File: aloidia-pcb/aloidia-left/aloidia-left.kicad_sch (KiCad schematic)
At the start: 81 parts

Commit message: Finished schematics of left half
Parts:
- removed J?: SWD 10 Pin 0.05", 0_various:FTSH-105-01, symbol 0_various:SWD 10 Pin 0.05"
- added C10, C11, C12, C13: 0.1uF, symbol Device:C_Small
- added D100, D101, D102, D103, D104, D105, D106, D107, D108, D110, D111, D112, D113, D114, D115, D116, D117, D120, D121, D122, D123, D124, D125, D126, D127, D130, D131, D132, D133, D134, D135, D136, D137, D140, D141, D142, D143, D144, D145, D146, D147, D2, D3, D4, D5, D6: 1N4148W, Diode_SMD:D_SOD-123, symbol Diode:1N4148W
- added FB2: MH2029-600Y, Inductor_SMD:L_0805_2012Metric, symbol 0_protection:MH2029-600Y
- added H1: 3.2mm_M3, MountingHole:MountingHole_3.2mm_M3_Pad_Via, symbol Mechanical:MountingHole_Pad
- added H2, H3, H4: 3.2mm_M3, MountingHole:MountingHole_3.2mm_M3_Pad_Via, symbol Mechanical:MountingHole
- added J1: SWD_02x05_1.27mm, 0_various:FTSH-105-01, symbol 0_various:SWD_02x05_1.27mm
- added J2: Pin headers 2.54mm 01x08, Connector_PinHeader_2.54mm:PinHeader_1x08_P2.54mm_Vertical, symbol Connector_Generic:Conn_01x08
- added J3: SM06B-SRSS-TB, Connector_JST:JST_SH_SM06B-SRSS-TB_1x06-1MP_P1.00mm_Horizontal, symbol Connector_Generic:Conn_01x06
- added R6, R7: 10k, symbol Device:R_Small
- added SW100: MX_EC11, 0_mx:MX_HS_AS_EC11_1u, symbol Device:RotaryEncoder_Switch
- added SW101, SW102, SW103, SW104, SW105, SW106, SW107, SW108, SW110, SW111, SW112, SW113, SW114, SW115, SW116, SW117, SW120, SW121, SW122, SW123, SW124, SW125, SW126, SW127, SW130, SW131, SW132, SW133, SW134, SW135, SW136, SW137, SW140, SW141, SW142, SW143, SW144, SW145, SW146, SW243, SW244, SW246: SW_Push, symbol Switch:SW_Push
- added SW2: MX_EVQWGD001, 0_mx:MX_HS_AS_1u_EVQWGD001, symbol Device:RotaryEncoder_Switch
- added SW4: EG6201, 0_switch_button:SW_EG6201, symbol 0_switch_button:EG6201
- added TP1: 3.3V, 0_various:TestPoint, symbol Connector:TestPoint
- added TP10: SDA, 0_various:TestPoint, symbol Connector:TestPoint
- added TP11: EVQ_ENCB, 0_various:TestPoint, symbol Connector:TestPoint
- added TP12: EVQ_ENCA, 0_various:TestPoint, symbol Connector:TestPoint
- added TP13: EC_ENCB, 0_various:TestPoint, symbol Connector:TestPoint
- added TP14: EC_ENCA, 0_various:TestPoint, symbol Connector:TestPoint
- added TP15: RESET, 0_various:TestPoint, symbol Connector:TestPoint
- added TP16: ROW0, 0_various:TestPoint, symbol Connector:TestPoint
- added TP17: ROW1, 0_various:TestPoint, symbol Connector:TestPoint
- added TP18: ROW2, 0_various:TestPoint, symbol Connector:TestPoint
- added TP19: ROW3, 0_various:TestPoint, symbol Connector:TestPoint
- added TP2: VDD, 0_various:TestPoint, symbol Connector:TestPoint
- added TP20: ROW4, 0_various:TestPoint, symbol Connector:TestPoint
- added TP21: COL0, 0_various:TestPoint, symbol Connector:TestPoint
- added TP22: COL1, 0_various:TestPoint, symbol Connector:TestPoint
- added TP23: COL2, 0_various:TestPoint, symbol Connector:TestPoint
- added TP24: COL6, 0_various:TestPoint, symbol Connector:TestPoint
- added TP25: COL7, 0_various:TestPoint, symbol Connector:TestPoint
- added TP26: COL8, 0_various:TestPoint, symbol Connector:TestPoint
- added TP27: COL9, 0_various:TestPoint, symbol Connector:TestPoint
- added TP28, TP29, TP30, TP31, TP32: GND, lib_fp:TestPoint, symbol Connector:TestPoint
- added TP3: VDDH, 0_various:TestPoint, symbol Connector:TestPoint
- added TP33: COL3, 0_various:TestPoint, symbol Connector:TestPoint
- added TP34: COL4, 0_various:TestPoint, symbol Connector:TestPoint
- added TP35: COL5, 0_various:TestPoint, symbol Connector:TestPoint
- added TP4: VBUS, 0_various:TestPoint, symbol Connector:TestPoint
- added TP5: VBUS_ESD, 0_various:TestPoint, symbol Connector:TestPoint
- added TP6: VBUS_FUSE, 0_various:TestPoint, symbol Connector:TestPoint
- added TP7: SYSOFF, 0_various:TestPoint, symbol Connector:TestPoint
- added TP8: CHG, 0_various:TestPoint, symbol Connector:TestPoint
- added TP9: SCL, 0_various:TestPoint, symbol Connector:TestPoint
- D1: renamed from D?; value LED_BGRA -> IN-P32TRRRGB; footprint (none) -> 0_various:IN-P32TRRRGB; Manufacturer ref (none) -> IN-P32TRRRGB; Mouser ref (none) -> 743-IN-P32TRRRGB
- R10: renamed from R?; value 10k -> 1.27k
- R11: renamed from R?; value 10k -> 1.15k
- R12: renamed from R?; value 10k -> 1.4k
- gave numbers to parts that had none: 69
- renumbered RESET to RESET1
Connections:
- net +3.3V: now also J2.2 (Pin_2), TP1.1
- net CHG: now also TP8.1
- net D+: no longer U7.6 (IO4)
- net D-: no longer U7.4 (IO3)
- net GND: now also C10.2, C11.1, C12.2, C13.1, FB2.2, J1.3 (GND), J1.5 (GND), J2.1 (Pin_1), SW100.C, SW2.C, SW4.18, SW4.S1 (SHIELD), SW4.S2 (SHIELD), SW4.S3 (SHIELD), SW4.S4 (SHIELD), TP28.1, TP29.1, TP30.1, TP31.1, TP32.1
- net RESET: now also J1.10 (nRESET), TP15.1
- net SCL: now also U2.26 (TRACEDATA3/P1.09), R6.2, TP9.1
- net SDA: now also U2.27 (TRACEDATA2/P0.11), R7.2, TP10.1
- net SWCLK: now also J1.4 (SWCLK/TCK)
- net SWDIO: now also J1.2 (SWDIO/TMS)
- net SWO: now also J1.6 (SWO/TDO)
- net SYSOFF: now also TP7.1
- net VBUS: now also TP4.1
- net VBUS_FUSE: now also TP6.1
- net VDDH: now also TP3.1
- net VDD_nrf: now also J1.1 (VTref), R6.1, R7.1, TP2.1
- net AP_VDD: now reaches C16.1, R17.2, U6.5 (VDD)
- net VBAT_UV: now reaches RUV1.2, RUV2.1, U8.8 (VBAT_UV)
- net VOC_SAMP: now reaches ROC1.1, ROC2.2, U8.3 (VOC_SAMP)
- net VSTOR: now reaches C19.1, C21.1, U8.15 (VSTOR)
- net DO: now reaches Q2.4 (G2), U6.1 (DO)
- net CO: now reaches Q2.6 (G1), U6.3 (CO)
- net VM: now reaches R18.1, U6.2 (VM)
- net VREF_SAMP: now reaches C18.1, U8.4 (VREF_SAMP)
- net COL8: now reaches U2.10 (P0.29/AIN5)
- net COL8: now also SW108.2, TP26.1
- net COL7: now reaches U2.11 (P0.02/AIN0)
- net COL7: now also SW107.2, SW117.2, SW127.2, SW137.2, SW2.S2, SW4.3, TP25.1
- net COL6: now reaches U2.12 (P0.31/AIN7)
- net COL6: now also SW106.2, SW116.2, SW126.2, SW136.2, SW146.2, SW246.2, TP24.1
- net COL5: now reaches U2.13 (P0.28/AIN4)
- net COL5: now also SW105.2, SW115.2, SW125.2, SW135.2, SW145.2, TP35.1
- net COL4: now reaches U2.14 (P0.30/AIN6)
- net COL4: now also SW104.2, SW114.2, SW124.2, SW134.2, SW144.2, SW244.2, TP34.1
- net EVQ_ENCB: now reaches U2.22 (P0.06)
- net EVQ_ENCB: now also C12.1, SW2.B, SW4.9, TP11.1
- net EVQ_ENCA: now reaches U2.24 (P0.08)
- net EVQ_ENCA: now also C13.2, SW2.A, SW4.12, TP12.1
- net COL3: now reaches U2.36 (P0.14)
- net COL3: now also SW103.2, SW113.2, SW123.2, SW133.2, SW143.2, SW243.2, TP33.1
- net COL2: now reaches U2.37 (P0.13)
- net COL2: now also SW102.2, SW112.2, SW122.2, SW132.2, SW142.2, TP23.1
- net COL1: now reaches U2.38 (P0.16)
- net COL1: now also SW101.2, SW111.2, SW121.2, SW131.2, SW141.2, TP22.1
- net COL0: now reaches U2.39 (P0.15)
- net COL0: now also SW100.S2, SW110.2, SW120.2, SW130.2, SW140.2, TP21.1
- net ROW4: now reaches U2.4 (P1.11)
- net ROW4: now also D140.2 (A), D141.2 (A), D142.2 (A), D143.2 (A), D144.2 (A), D145.2 (A), D146.2 (A), D147.2 (A), D6.2 (A)
- net DIN: now reaches U2.41 (P0.17)
- net DIN: now also J2.3 (Pin_3)
- net SCK: now reaches U2.42 (P0.19)
- net SCK: now also J2.4 (Pin_4)
- net CS: now reaches U2.43 (P0.21)
- net CS: now also J2.5 (Pin_5)
- net DC: now reaches U2.44 (P0.20)
- net DC: now also J2.6 (Pin_6)
- net RST: now reaches U2.45 (P0.23)
- net RST: now also J2.7 (Pin_7)
- net BUSY: now reaches U2.46 (P0.22)
- net BUSY: now also J2.8 (Pin_8)
- net EC_ENCB: now reaches U2.48 (P0.24)
- net EC_ENCB: now also C10.1, SW100.B, TP13.1
- net EC_ENCA: now reaches U2.49 (P0.25)
- net EC_ENCA: now also C11.2, SW100.A, TP14.1
- net ROW3: now reaches U2.5 (P1.12)
- net ROW3: now also D130.2 (A), D131.2 (A), D132.2 (A), D133.2 (A), D134.2 (A), D135.2 (A), D136.2 (A), D137.2 (A), D5.2 (A), TP19.1, TP20.1
- net ROW2: now reaches U2.6 (P1.13)
- net ROW2: now also D120.2 (A), D121.2 (A), D122.2 (A), D123.2 (A), D124.2 (A), D125.2 (A), D126.2 (A), D127.2 (A), D4.2 (A), TP18.1
- net ROW1: now reaches U2.7 (P1.14)
- net ROW1: now also D110.2 (A), D111.2 (A), D112.2 (A), D113.2 (A), D114.2 (A), D115.2 (A), D116.2 (A), D117.2 (A), D3.2 (A), TP17.1
- net ROW0: now reaches U2.8 (P1.15)
- net ROW0: now also D100.2 (A), D101.2 (A), D102.2 (A), D103.2 (A), D104.2 (A), D105.2 (A), D106.2 (A), D107.2 (A), D108.2 (A), D2.2 (A), TP16.1
- net COL9: now reaches U2.9 (P0.03/AIN1)
- net COL9: now also SW4.1, TP27.1
- net VRDIV: now reaches ROV2.2, RUV2.2, U8.7 (VRDIV)
- net VBAT_OV: now reaches ROV1.2, ROV2.1, U8.6 (VBAT_OV)
- net at FB1.1: now also H1.1; no longer J7.S1 (SHIELD)
- net LBST: now reaches L2.2, U8.16 (LBST)
- net LTC_S renamed VBUS_ESD
- net VBUS_ESD: now also TP5.1
- new net: D127.1 (K), SW127.1
- new net: D144.1 (K), SW144.1, SW244.1
- new net: D122.1 (K), SW122.1
- new net: D136.1 (K), SW136.1
- new net: D142.1 (K), SW142.1
- new net: D145.1 (K), SW145.1
- new net: D114.1 (K), SW114.1
- new net: D133.1 (K), SW133.1
- new net: D2.1 (K), SW4.4
- new net: D135.1 (K), SW135.1
- new net: D112.1 (K), SW112.1
- new net: D134.1 (K), SW134.1
- new net: D102.1 (K), SW102.1
- new net: D124.1 (K), SW124.1
- new net: D137.1 (K), SW137.1
- new net: D111.1 (K), SW111.1
- new net: D4.1 (K), SW4.10
- new net: J3.4 (Pin_4), SW4.11
- new net: D5.1 (K), SW4.13
- new net: J3.5 (Pin_5), SW4.14
- new net: D6.1 (K), SW4.16
- new net: J3.6 (Pin_6), SW4.17
- new net: J3.1 (Pin_1), SW4.2
- new net: J3.2 (Pin_2), SW4.5
- new net: D3.1 (K), SW4.7
- new net: J3.3 (Pin_3), SW4.8
- new net: D104.1 (K), SW104.1
- new net: D125.1 (K), SW125.1
- new net: D120.1 (K), SW120.1
- new net: D116.1 (K), SW116.1
- new net: D121.1 (K), SW121.1
- new net: D100.1 (K), SW100.S1
- new net: D108.1 (K), SW108.1
- new net: D113.1 (K), SW113.1
- new net: D103.1 (K), SW103.1
- new net: FB2.1, J7.S1 (SHIELD)
- new net: D106.1 (K), SW106.1
- new net: D141.1 (K), SW141.1
- new net: D101.1 (K), SW101.1
- new net: D132.1 (K), SW132.1
- new net: D146.1 (K), SW146.1, SW246.1
- new net: D123.1 (K), SW123.1
- new net: D143.1 (K), SW143.1, SW243.1
- new net: D140.1 (K), SW140.1
- new net: D107.1 (K), SW107.1
- new net: D105.1 (K), SW105.1
- new net: D126.1 (K), SW126.1
- new net: D131.1 (K), SW131.1
- new net: D117.1 (K), SW117.1
- new net: D110.1 (K), SW110.1
- new net: D130.1 (K), SW130.1
- new net: D115.1 (K), SW115.1
- new net ROW4_SW: D147.1 (K), SW2.S1, SW4.6
- no-connect marks 15 -> 34
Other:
- note added: "3.3V LDO"
- note added: "Battery Charger"
- note added: "Battery Connectors"
- note added: "CL = 12.5 pF CPIN ~ 4 pF CPCB ~ 5 pF C1' = C2' = C' = 2*CL = 25 pF C1 = C2 = C' - CPCB - CPIN = 25 pF - 4 pF - 5 pF = 16 pF"
- note added: "Daugtherboard connector"
- note added: "Debug"
- note added: "E-ink Display Module Connector"
- note added: "Energy Harvester"
- note added: "Fuel Gauge"
- note added: "Low freq pins: P1.01-07 P1.10-15 P0.02-03 P0.09-10 P0.28-31"
- note added: "MX Switch + EC11 Encoder"
- note added: "MX Switch + Horizontal Encoder"
- note added: "MX Switch EC11 enc"
- note added: "MX Switch Horiz enc Nav switch"
- note added: "Mounting Holes"
- note added: "Navigation switch/Encoder selection"
- note added: "Power Flags"
- note added: "Power Path"
- note added: "Reset"
- note added: "Status/Charge RGB LED"
- note added: "Switch Matrix"
- note added: "Test Points"
- note added: "To 5-way navigation switch"
- note added: "To horizontal encoder"
- note added: "USB-C Input"
- note added: "USB-C Remote"
- note added: "Y = 0.59G + 0.30R + 0.11B Green: If_G = 2.0 mA @ 12 % rel. luminous intensity Iv_G = 0.12 * 2000 mcd = 240 mcd Iv_tot = 240 mcd / 0.59 = 407 mcd Red: Iv_R = 0.30 * 407 = 122 mcd Iv_R / Iv_R_nom = 122 mcd / 600 mcd = 0.20 If_R = 2.5 mA @ 20 % rel. luminous intensity Blue:: Iv_B = 0.11 * 407 = 45 mcd Iv_B / Iv_B_nom = 45 mcd / 450 mcd = 0.10 If_B = 1.8 mA @ 10 % rel. luminous intensity R_G = (VDDH 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"
- note added: "nRF52840 Module (MDBT50Q-1MV2)"
- note removed: "CL = 12.5pF CPIN ~ 4pF CPCB ~ 5pF C1' = C2' = C' = 2*CL = 25pF C1 = C2 = C' - CPCB - CPIN = 25 - 4 - 5 = 16pF"
- note removed: "TODO: 6pdt switch external pullup on i2c? remove prot on remote usb add matrix add e-paper connector"
- title: (none) -> ALOIDIA Keyboard Left Side
- moved on the sheet: C1, C14, C15, C16, C17, C18, C19, C2, C20, C21, C3, C4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

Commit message: Assigned all footprints
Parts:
- added S132, S146: MX_stab, marbastlib-mx:STAB_MX_P_2.25u, symbol marbastlib-mx:MX_stab
- added S246: MX_stab, marbastlib-mx:STAB_MX_P_2.75u, symbol marbastlib-mx:MX_stab
- C1, C10, C11, C12, C13, C14, C15, C16, C17, C18, C19, C2, C20, C21, C3, C4, C5, C6, C7, C8, C9: footprint (none) -> Capacitor_SMD:C_0603_1608Metric
- J1: Manufacturer ref Adafruit 4048 -> 4048; Mouser ref (none) -> 485-4048
- J10, J2, J6: now left out of the parts list
- JP1, JP2: footprint (none) -> Jumper:SolderJumper-2_P1.3mm_Open_RoundedPad1.0x1.5mm
- L1, L2: footprint (none) -> Inductor_SMD:L_0603_1608Metric
- R1, R10, R11, R12, R13, R14, R15, R16, R17, R18, R19, R2, R20, R21, R3, R4, R5, R6, R7, R8, R9, ROC1, ROC2, ROV1, ROV2, RUV1, RUV2: footprint (none) -> Resistor_SMD:R_0603_1608Metric
- SW101, SW102, SW103, SW104, SW105, SW106, SW107, SW108, SW110, SW111, SW113, SW114, SW115, SW116, SW117, SW120, SW121, SW123, SW124, SW125, SW126, SW127, SW130, SW131, SW132, SW133, SW134, SW135, SW136, SW137, SW140, SW141, SW145, SW146, SW243, SW246: footprint (none) -> 0_mx:MX_HS_AS_1u
- SW112, SW144: footprint (none) -> 0_mx:MX_HS_AS_1.5u
- SW122: footprint (none) -> 0_mx:MX_HS_AS_1.75u
- SW142, SW143, SW244: footprint (none) -> 0_mx:MX_HS_AS_1.25u
- TP28, TP29, TP30, TP31, TP32: footprint lib_fp:TestPoint -> 0_various:TestPoint
- U4: Digikey ref (none) -> DMN2004DMKDICT-ND; Manufacturer ref (none) -> DMN2004DMK-7
- U8: Manufacturer ref (none) -> BQ25504RGTR; Mouser ref (none) -> 595-BQ25504RGTR
- Y1: footprint (none) -> Crystal:Crystal_SMD_MicroCrystal_CM9V-T1A-2Pin_1.6x1.0mm
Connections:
- net CC1: now also R20.1; no longer R20.2
- net CC2: now also R19.1; no longer R19.2
- net GND: now also R19.2, R20.2; no longer R19.1, R20.1
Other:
- note added: "(EN2, EN1) = (VDDH, GND) -> Max Input Current = 500 mA ISET: R_ISET = K_ISET/I_CHG = 890 AOhm / 0.5 A = 1.8 kOhm (1% tol) TMR: R_TMR = t_MAXCHG/(10*K_TMR) = 3 * 3600 s / (10 * 48 s/kOhm) = 22.5 kOhm -> 22 kOhm ILIM: R_ILIM = K_ILIM/ILIM = 1610 AOhm / 0.6 A = 2.7 k Ohm Note: R_ILIM can be chosen for any value between 1.1 kOhm to 8 kOhm because USB500 mode is enabled"
- note removed: "(EN2, EN1) = (0, 1) -> Max Input Current = 500mA ISET: R_ISET = K_ISET/I_CHG = 890 AOhm / 0.5 A = 1.8 kOhm (1% tol) TMR: R_TMR = t_MAXCHG/(10*K_TMR) = 3*3600 s / (10*48 s/kOhm) = 22.5 kOhm -> 22 kOhm ILIM: R_ILIM = K_ILIM/ILIM = 1610 AOhm / 0.6 A = 2.7 k Ohm Note: R_ILIM can be chosen for any value between 1.1 kOhm to 8 kOhm because USB500 mode is enabled"
- moved on the sheet: C17, J10, J9, RUV1, RUV2

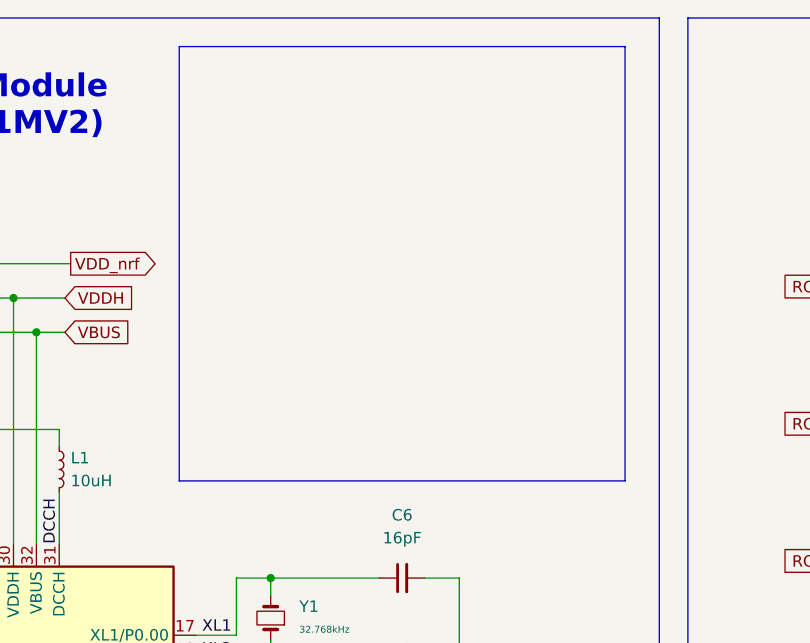
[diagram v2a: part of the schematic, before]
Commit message: Added design rules, net classes constraints and all footprint 3d models
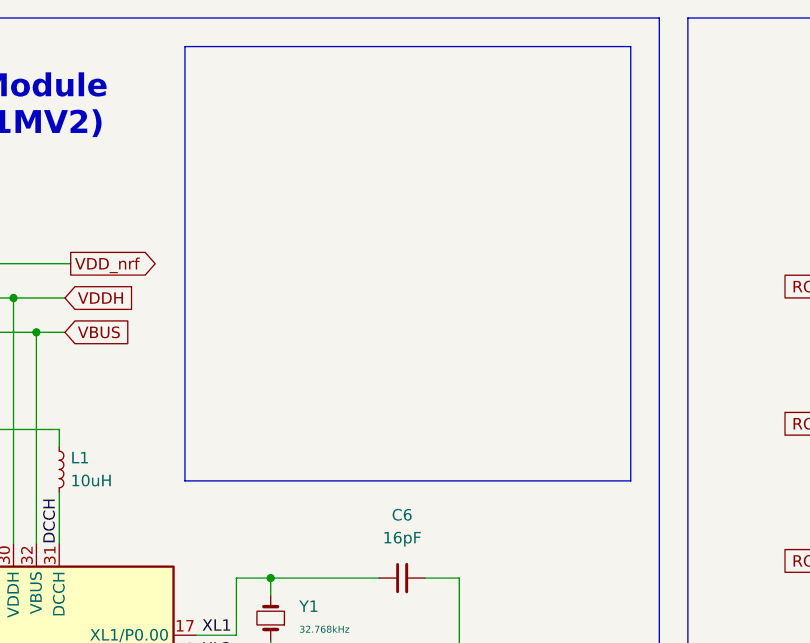
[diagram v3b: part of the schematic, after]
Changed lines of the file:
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@@
     (stroke (width 0) (type default) (color 0 0 0 0))
   )
-  (polyline (pts (xy 91.44 18.415) (xy 91.44 66.675))
+  (polyline (pts (xy 92.075 18.415) (xy 92.075 66.675))
     (stroke (width 0) (type default) (color 0 0 0 0))
   )
@@
     (stroke (width 0) (type default) (color 0 0 0 0))
   )
-  (polyline (pts (xy 91.44 18.415) (xy 140.97 18.415))
+  (polyline (pts (xy 92.075 18.415) (xy 141.605 18.415))
     (stroke (width 0) (type default) (color 0 0 0 0))
   )
@@
     (stroke (width 0) (type default) (color 0 0 0 0))
   )
-  (polyline (pts (xy 140.97 66.675) (xy 91.44 66.675))
+  (polyline (pts (xy 141.605 66.675) (xy 92.075 66.675))
     (stroke (width 0) (type default) (color 0 0 0 0))
   )
@@
     (stroke (width 0) (type default) (color 0 0 0 0))
   )
-  (polyline (pts (xy 140.97 18.415) (xy 140.97 66.675))
+  (polyline (pts (xy 141.605 18.415) (xy 141.605 66.675))
     (stroke (width 0) (type default) (color 0 0 0 0))
   )
@@
     (stroke (width 0) (type default) (color 0 0 0 0))
   )
-  (image (at 116.205 42.545) (scale 0.897509)
+  (image (at 116.84 42.545) (scale 0.897509)
     (data
       iVBORw0KGgoAAAANSUhEUgAAAowAAAJ5CAIAAACrDvYrAAAAA3NCSVQICAjb4U/gAAAACXBIWXMA

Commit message: Routed left side
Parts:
- removed J8: SM04B-SRSS-TB(LF)(SN), Connector_JST:JST_SH_SM04B-SRSS-TB_1x04-1MP_P1.00mm_Horizontal, symbol Connector_Generic:Conn_01x04
- removed SW3: SSSS213100, marbastlib-various:SW_SSSS213100, symbol Switch:SW_SPDT
- removed TP1: 3.3V, 0_various:TestPoint, symbol Connector:TestPoint
- added D11: IN-P32TRRRGB, 0_various:IN-P32TRRRGB, symbol Device:LED_BGRA
- added H5, H6: 3.2mm_M3, MountingHole:MountingHole_3.2mm_M3_Pad, symbol Mechanical:MountingHole
- added J12: Pin headers 2.54mm 01x08, Connector_PinHeader_2.54mm:PinHeader_1x08_P2.54mm_Vertical, symbol Connector_Generic:Conn_01x08
- added JP3: NO_THERM, Jumper:SolderJumper-2_P1.3mm_Open_TrianglePad1.0x1.5mm, symbol Jumper:Jumper_2_Open
- H1: footprint MountingHole:MountingHole_3.2mm_M3_Pad_Via -> MountingHole:MountingHole_3.2mm_M3_Pad
- H2, H3, H4: footprint MountingHole:MountingHole_3.2mm_M3_Pad_Via -> MountingHole:MountingHole_3.2mm_M3_Pad; now left out of the parts list
- JP1: value OVCH_DISABLE -> REV_PROT_DISABLE; footprint Jumper:SolderJumper-2_P1.3mm_Open_RoundedPad1.0x1.5mm -> Jumper:SolderJumper-2_P1.3mm_Open_TrianglePad1.0x1.5mm; now left out of the parts list
- JP2: footprint Jumper:SolderJumper-2_P1.3mm_Open_RoundedPad1.0x1.5mm -> Jumper:SolderJumper-2_P1.3mm_Open_TrianglePad1.0x1.5mm; now left out of the parts list
- L2: footprint Inductor_SMD:L_0603_1608Metric -> Inductor_SMD:L_1210_3225Metric
- S132, S146: footprint marbastlib-mx:STAB_MX_P_2.25u -> marbastlib-mx:STAB_MX_2.25u
- S246: footprint marbastlib-mx:STAB_MX_P_2.75u -> marbastlib-mx:STAB_MX_2.75u
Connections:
- net TS is gone; now on net NTC: U5.1 (TS)
- net +3.3V: now also J12.2 (Pin_2)
- net -BATT: now also Q2.1 (D1); no longer Q2.3 (S2)
- net BUSY: now also J12.8 (Pin_8)
- net CO: now also Q2.4 (G2); no longer Q2.6 (G1)
- net COL3: now also SW143.1; no longer SW143.2
- net COL4: now also SW144.1, U2.13 (P0.28/AIN4); no longer SW144.2, U2.14 (P0.30/AIN6)
- net COL5: now also U2.14 (P0.30/AIN6); no longer U2.13 (P0.28/AIN4)
- net COL6: now also SW246.1; no longer SW246.2
- net COL9: now also U2.4 (P1.11); no longer U2.9 (P0.03/AIN1)
- net CS: now also J12.5 (Pin_5)
- net D-: now also U7.6 (IO4); no longer U7.3 (IO2)
- net DC: now also J12.6 (Pin_6)
- net DIN: now also J12.3 (Pin_3)
- net DO: now also Q2.6 (G1); no longer Q2.4 (G2)
- net EC_ENCA: now also U2.48 (P0.24); no longer U2.49 (P0.25)
- net EC_ENCB: now also U2.49 (P0.25); no longer U2.48 (P0.24)
- net GND: now also Q2.3 (S2), J12.1 (Pin_1); no longer Q2.1 (D1)
- net NTC: now also JP3.1 (A)
- net ROW0: now also D3.2 (A), U2.9 (P0.03/AIN1); no longer D2.2 (A), U2.8 (P1.15)
- net ROW1: now also D6.2 (A), U2.8 (P1.15); no longer D3.2 (A), U2.7 (P1.14)
- net ROW2: now also D2.2 (A), U2.7 (P1.14); no longer D4.2 (A), U2.6 (P1.13)
- net ROW3: now also U2.6 (P1.13); no longer TP20.1, U2.5 (P1.12)
- net ROW4: now also D4.2 (A), TP20.1, U2.5 (P1.12); no longer D6.2 (A), U2.4 (P1.11)
- net ROW4_SW: now also D4.1 (K), SW4.10, SW4.15; no longer SW4.6
- net RST: now also J12.7 (Pin_7)
- net SCK: now also J12.4 (Pin_4)
- net VDDH: now also D11.4 (A)
- net at D144.1 (K), SW244.1: now also SW144.2; no longer SW144.1
- net at R16.1: now also JP3.2 (B)
- net ROW2_SW: now reaches D2.1 (K), SW4.4
- net LTC_VSS: now reaches R21.1, U9.6 (Vss)
- net ROW3_SW: now reaches D5.1 (K), SW4.13
- net ROW1_SW: now reaches D6.1 (K), SW4.16
- net at SW4.2: now also J3.3 (Pin_3); no longer J3.1 (Pin_1)
- net ROW0_SW: now reaches D3.1 (K), SW4.7
- net at SW4.8: now also J3.1 (Pin_1); no longer J3.3 (Pin_3)
- net D1/D2: now reaches Q2.2 (S1/D2), Q2.5 (S1/D2)
- net LED_BLUE_D: now reaches R10.1, U4.3 (D1)
- net LED_B: now reaches D1.1 (BK), R10.2
- net LED_B: now also D11.1 (BK)
- net LED_GREEN_D: now reaches R11.1, U4.6 (D2)
- net SHIELD: now reaches FB2.1, J7.S1 (SHIELD)
- net PP_G: now reaches Q1.1 (G), R4.2
- net at D146.1 (K), SW146.1: now also SW246.2; no longer SW246.1
- net LED_G: now reaches D1.2 (GK), R11.2
- net LED_G: now also D11.2 (GK)
- net LED_R: now reaches D1.3 (RK), R12.2
- net LED_R: now also D11.3 (RK)
- net at D143.1 (K), SW243.1: now also SW143.2; no longer SW143.1
- net +BATT_PULLUP: now reaches R5.2, SW1.1 (A)
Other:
- note added: "20431"
- note added: "Only populate one of the LED, depending on the chosen layout"
- note removed: "Daugtherboard connector"
- moved on the sheet: D1, D2, D3, D4, D5, D6, FB2, J2, Q2, R1, R4, R8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

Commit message: Added e-Paper display mechanical footprint
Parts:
- J12, J2: footprint Connector_PinHeader_2.54mm:PinHeader_1x08_P2.54mm_Vertical -> 0_various:e-Paper Display
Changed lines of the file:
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@@
       (effects (font (size 1.27 1.27)) (justify left))
     )
-    (property "Footprint" "Connector_PinHeader_2.54mm:PinHeader_1x08_P2.54mm_Vertical" (id 2) (at 300.99 347.345 0)
+    (property "Footprint" "0_various:e-Paper Display" (id 2) (at 300.99 347.345 0)
       (effects (font (size 1.27 1.27)) hide)
     )
@@
       (effects (font (size 1.27 1.27)) (justify left))
     )
-    (property "Footprint" "Connector_PinHeader_2.54mm:PinHeader_1x08_P2.54mm_Vertical" (id 2) (at 300.99 378.46 0)
+    (property "Footprint" "0_various:e-Paper Display" (id 2) (at 300.99 378.46 0)
       (effects (font (size 1.27 1.27)) hide)
     )
@@
     )
     (path "/1cda5eb4-afc8-4a02-b490-49ad1887b50a"
-      (reference "J2") (unit 1) (value "Pin headers 2.54mm 01x08") (footprint "Connector_PinHeader_2.54mm:PinHeader_1x08_P2.54mm_Vertical")
+      (reference "J2") (unit 1) (value "Pin headers 2.54mm 01x08") (footprint "0_various:e-Paper Display")
     )
     (path "/962e543a-c7cf-4094-9c46-8a755fd990cd"
@@
     )
     (path "/edd06817-62ac-4ee9-8cbf-ee1b8fa0a003"
-      (reference "J12") (unit 1) (value "Pin headers 2.54mm 01x08") (footprint "Connector_PinHeader_2.54mm:PinHeader_1x08_P2.54mm_Vertical")
+      (reference "J12") (unit 1) (value "Pin headers 2.54mm 01x08") (footprint "0_various:e-Paper Display")
     )
     (path "/6cdd3c99-5837-4b31-8029-55819d65dd32"
